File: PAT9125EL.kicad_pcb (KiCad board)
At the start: 2 copper layers, 4.9 x 10.4 mm, 9 parts, among them J1 Conn_01x06_Socket, U1 PAT9125EL

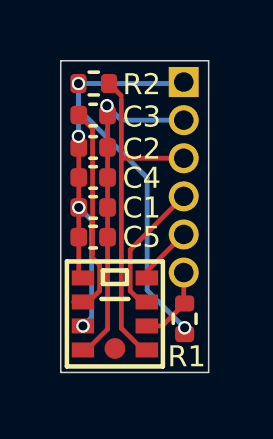
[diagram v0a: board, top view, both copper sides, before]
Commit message: shorten 1.5mm
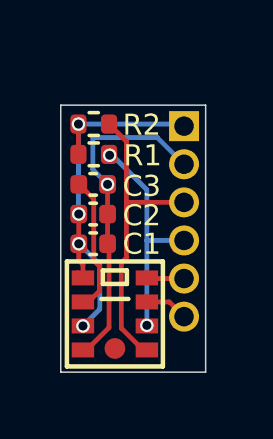
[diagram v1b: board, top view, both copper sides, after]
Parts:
- removed C4: 10uF, Capacitor_SMD:C_0402_1005Metric
- removed C5: 0.1uF, Capacitor_SMD:C_0402_1005Metric
- moved R1 6.26 mm to (146.4, 92.6), turned to 0 degrees
- moved C3 2.31 mm to (146.4, 93.6)
- moved C2 2.22 mm to (146.4, 94.6)
- moved J1 1.47 mm to (149.4, 91.7)
- moved R2 1.35 mm to (146.4, 91.6)
- moved C1 1.21 mm to (146.4, 95.6)
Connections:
- J1 pad 4: MOTION -> SDA
- J1 pad 6: SDA -> MOTION
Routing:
- net VCC 3.3V: track 24.4 -> 15.8 mm, vias 5 -> 4
- net SDA: track 2.76 -> 8.29 mm, vias 0 -> 2
- net MOTION: track 4.72 -> 2.07 mm
- net Net-(U1-VDDA): track 7.06 -> 4.56 mm
- net SCL: track 11.5 -> 10.2 mm
- net NCS: track 1.98 -> 1.25 mm
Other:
- board size 4.9 x 10.4 mm -> 4.8 x 8.9 mm
- board text added: "v2"
- board text removed: "BY"
- board text removed: "PCB v1"
